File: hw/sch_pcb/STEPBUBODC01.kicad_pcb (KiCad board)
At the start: 2 copper layers, 40.1 x 30 mm, 18 parts, among them J1 HEADER_1x03, J2 HEADER_2x03_PARALLEL, J3 HEADER_1x03, J4 HEADER_1x03, J5 HEADER_2x03_PARALLEL, J6 HEADER_2x03_PARALLEL, U1 TPS631000DRLR

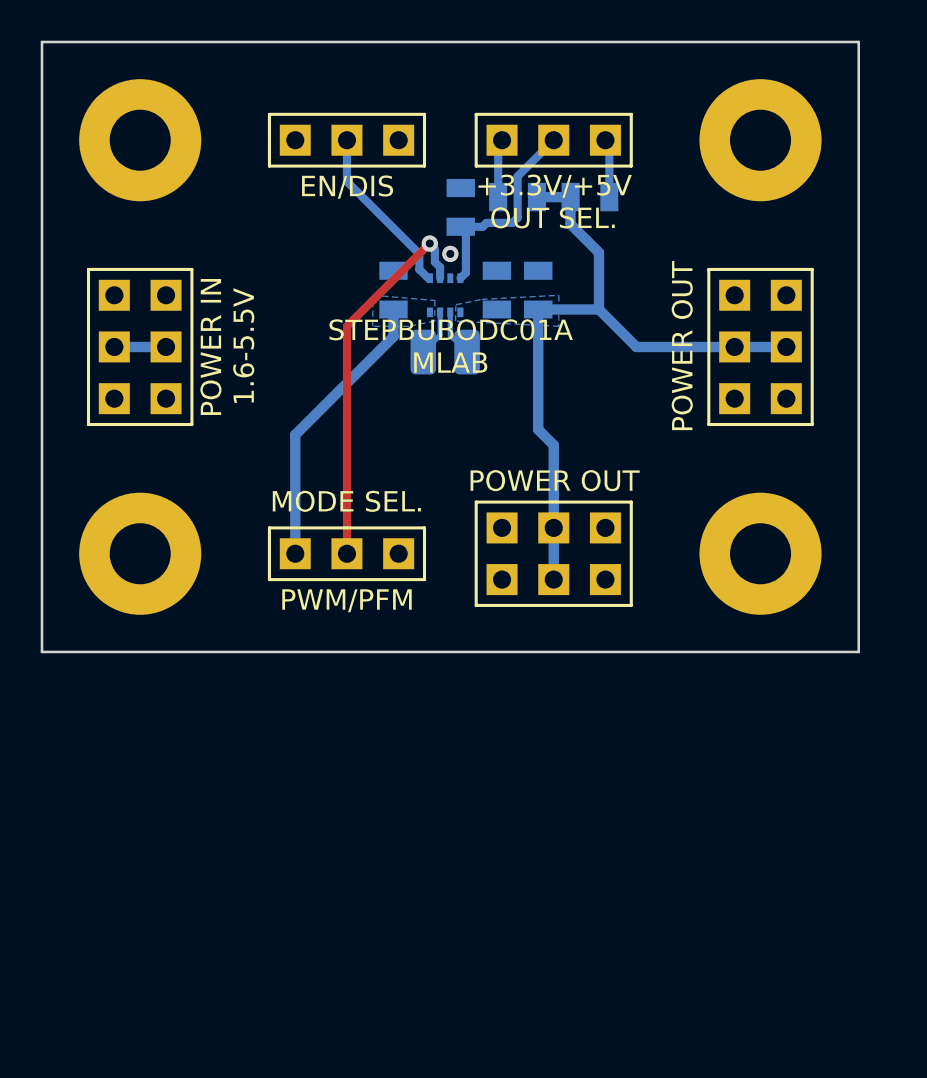
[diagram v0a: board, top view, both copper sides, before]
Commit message: Improvements in schematics and layout, solve: #1, #2, #4
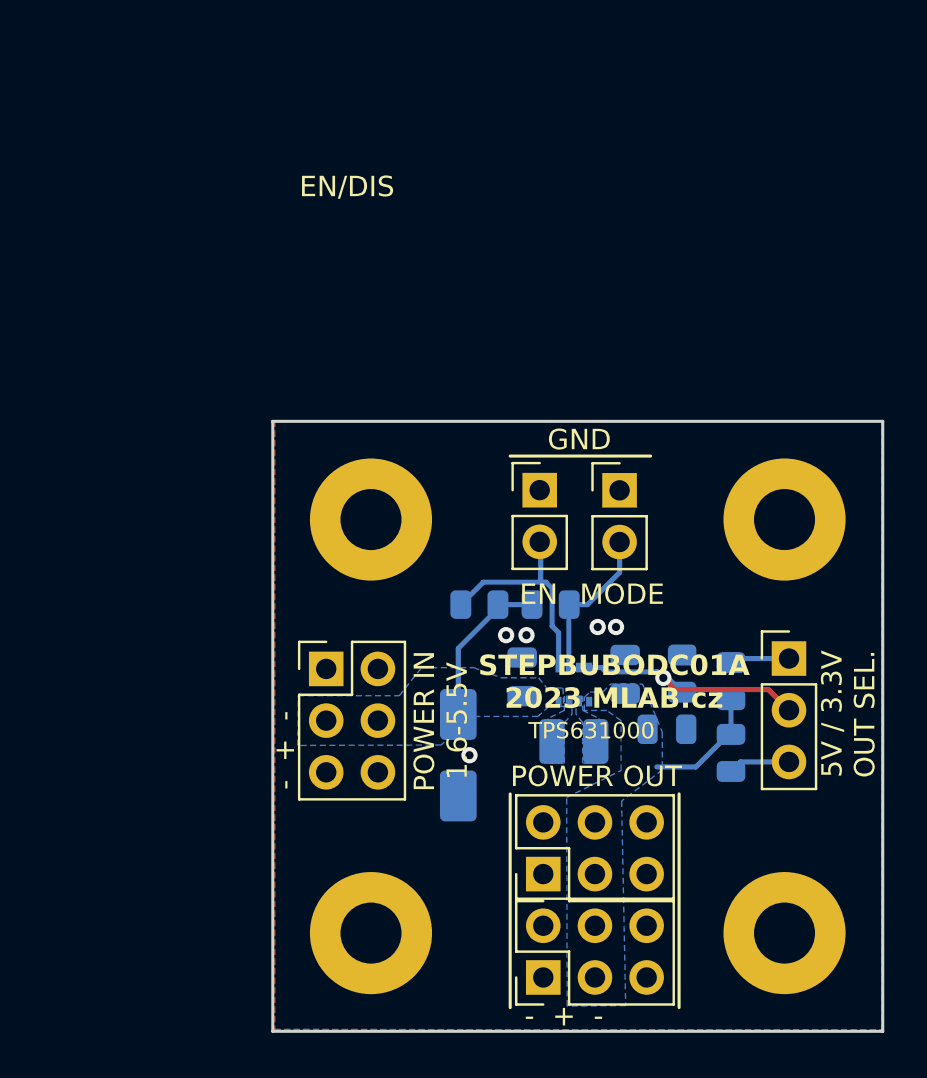
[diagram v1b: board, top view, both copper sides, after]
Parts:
- removed J1, J3: HEADER_1x03, Mlab_Pin_Headers:Straight_1x03
- added D1: M4, Diode_SMD:D_SMA, B.Cu at (142.6, 106.4)
- added JP1: Jumper_2_Open, Connector_PinHeader_2.54mm:PinHeader_1x02_P2.54mm_Vertical, F.Cu at (150.6, 93.4)
- added JP2: Jumper_2_Open, Connector_PinHeader_2.54mm:PinHeader_1x02_P2.54mm_Vertical, F.Cu at (146.6, 93.4)
- added R4: 1k, Resistor_SMD:R_0805_2012Metric, B.Cu at (147.2, 99.0)
- added R5: 1k, Resistor_SMD:R_0805_2012Metric, B.Cu at (143.7, 99.0)
- C1, C2, C3: footprint Mlab_C:SMD-0805 -> Capacitor_SMD:C_0805_2012Metric
- J2, J5, J6: footprint Mlab_Pin_Headers:Straight_2x03 -> Connector_PinHeader_2.54mm:PinHeader_2x03_P2.54mm_Vertical
- JP4: renamed from J4; footprint Mlab_Pin_Headers:Straight_1x03 -> Connector_PinHeader_2.54mm:PinHeader_1x03_P2.54mm_Vertical
- R1, R2, R3: footprint Mlab_R:SMD-0805 -> Resistor_SMD:R_0805_2012Metric
- moved H4 39.0 mm to (158.7, 115.2)
- moved R3 28.2 mm to (156.0, 106.3), turned to -90 degrees
- moved J6 28.0 mm to (146.8, 112.3), turned to 90 degrees
- moved JP4 28.0 mm to (158.9, 101.7), turned to 0 degrees
- moved R2 26.0 mm to (156.0, 102.8), turned to 90 degrees
- moved R1 25.4 mm to (153.6, 102.4)
- moved C3 22.5 mm to (152.9, 105.1), turned to 0 degrees
- moved H1 21.8 mm to (138.3, 94.8)
- moved H3 21.8 mm to (138.3, 115.2)
- moved J5 20.8 mm to (146.8, 117.3), turned to 90 degrees
- moved U1 20.1 mm to (148.3, 102.9)
- moved L1 20.1 mm to (148.3, 105.7)
- moved C1 20.0 mm to (145.8, 102.6)
- moved C2 19.9 mm to (150.8, 102.4)
- moved J2 18.3 mm to (136.1, 102.2)
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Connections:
- J2 pad 3: Net-(F1-Pad1) -> /V_in
- J2 pad 4: Net-(F1-Pad1) -> /V_in
- JP4 pad 1: Net-(J4-Pad1) -> /SEL_3v3
- JP4 pad 3: Net-(J4-Pad3) -> /SEL_5v
- R2 pad 2: Net-(J4-Pad3) -> /SEL_3v3
- R3 pad 2: Net-(J4-Pad1) -> /SEL_5v
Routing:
- net /V_out: track 34.5 -> 6.01 mm
- net /mod: track 18.8 -> 7.73 mm, vias 1 -> 0
- net /V_in: track 14.0 -> 6.59 mm
- net /SEL_5v: track 0.00 -> 3.04 mm
- net /SEL_3v3: track 0.00 -> 2.93 mm
- net Net-(J4-Pad3): track 2.87 -> 0.00 mm
- net Net-(J4-Pad1): track 2.87 -> 0.00 mm
- net Net-(F1-Pad1): track 2.54 -> 0.00 mm
- net /en: track 8.52 -> 11.0 mm
- net Net-(U1-LX2): track 2.30 -> 0.00 mm
- net Net-(U1-LX1): track 2.30 -> 0.00 mm
- net /FB: track 10.3 -> 11.9 mm, vias 0 -> 1
- net GND: track 0.00 -> 0.27 mm, vias 0 -> 5
- net (no net): vias 1 -> 0
- added copper zone on B.Cu, net GND
- added copper zone on F.Cu, net GND
- added copper zone on B.Cu, net Net-(U1-LX1)
- added copper zone on B.Cu, net Net-(U1-LX2)
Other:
- board size 40.1 x 30 mm -> 30 x 30 mm
- board text added: "- + -"
- board text added: "5V / 3.3V OUT SEL."
- board text added: "EN"
- board text added: "GND"
- board text added: "MODE"
- board text added: "STEPBUBODC01A 2023 MLAB.cz"
- board text added: "TPS631000"
- board text removed: "+3.3V/+5V OUT SEL."
- board text removed: "MODE SEL."
- board text removed: "PWM/PFM"
- board text removed: "STEPBUBODC01A MLAB"

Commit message: add fidu, check layout, drc, update ust_id
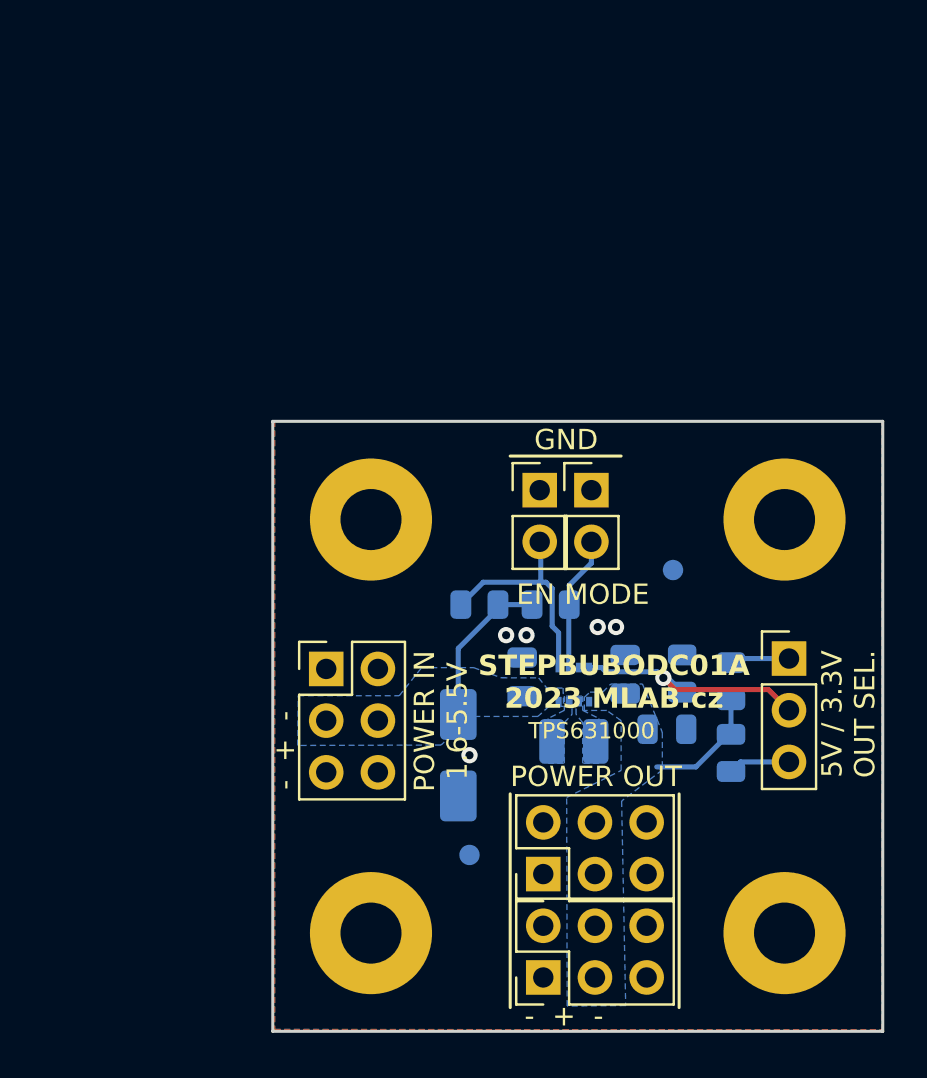
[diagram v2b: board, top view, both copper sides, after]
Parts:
- added FID1: Fiducial, Fiducial:Fiducial_1mm_Mask2mm, B.Cu at (143.2, 111.3)
- added FID2: Fiducial, Fiducial:Fiducial_1mm_Mask2mm, B.Cu at (153.2, 97.3)
- moved JP1 1.39 mm to (149.2, 93.4)
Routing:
- net /mod: track 7.73 -> 6.64 mm
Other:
- board text removed: "EN/DIS"

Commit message: Kontrola a opravy pred vyrobou
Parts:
- U1: footprint KiCad:SOTFL50P160X60-8N -> Mlab_IO:TPS631000
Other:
- rule pad_to_mask_clearance: 0 -> 0.2
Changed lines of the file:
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@@
   )
   (setup
-    (pad_to_mask_clearance 0)
+    (stackup
+      (layer "F.SilkS" (type "Top Silk Screen"))
+      (layer "F.Paste" (type "Top Solder Paste"))
+      (layer "F.Mask" (type "Top Solder Mask") (thickness 0.01))
+      (layer "F.Cu" (type "copper") (thickness 0.035))
+      (layer "dielectric 1" (type "core") (thickness 1.51) (material "FR4") (epsilon_r 4.5) (loss_tangent 0.02))
+      (layer "B.Cu" (type "copper") (thickness 0.035))
+      (layer "B.Mask" (type "Bottom Solder Mask") (thickness 0.01))
+      (layer "B.Paste" (type "Bottom Solder Paste"))
+      (layer "B.SilkS" (type "Bottom Silk Screen"))
+      (copper_finish "None")
+      (dielectric_constraints no)
+    )
+    (pad_to_mask_clearance 0.2)
     (aux_axis_origin 128.179999 125.32)
     (grid_origin 128.179999 125.32)
@@
     )
   )
-  (footprint "KiCad:SOTFL50P160X60-8N" (layer "B.Cu")
+  (footprint "Mlab_IO:TPS631000" (layer "B.Cu")
     (at 148.307999 102.949 90)
     (descr "DRL0008A")
@@
     (property "ki_description" "Switching Voltage Regulators 1.5-A output current, high power density buck-boost converter")
     (attr smd)
-    (fp_text reference "U1" (at 0 0 90) (layer "B.SilkS") hide
+    (fp_text reference "U1" (at 0 0 270) (layer "B.SilkS") hide
         (effects (font (size 1.27 1.27) (thickness 0.254)) (justify mirror))
     )
-    (fp_text value "TPS631000DRLR" (at 0 0 90) (layer "B.SilkS") hide
+    (fp_text value "TPS631000DRLR" (at 0 0 270) (layer "B.SilkS") hide
         (effects (font (size 1.27 1.27) (thickness 0.254)) (justify mirror))
     )
-    (fp_text user "${REFERENCE}" (at 0 0 90) (layer "B.Fab")
+    (fp_text user "${REFERENCE}" (at 0 0 270) (layer "B.Fab")
         (effects (font (size 1.27 1.27) (thickness 0.254)) (justify mirror))
     )
@@
     (fp_line (start 0.6 1.05) (end 0.6 -1.05)
       (stroke (width 0.1) (type solid)) (layer "B.Fab"))
-    (pad "1" smd rect (at -0.838 0.75) (size 0.3 0.475) (layers "B.Cu" "B.Paste" "B.Mask")
+    (pad "1" smd rect (at -0.74 0.75) (size 0.3 0.67) (layers "B.Cu" "B.Paste" "B.Mask")
       (net 3 "/V_out") (pinfunction "VOUT") (pintype "passive"))
-    (pad "2" smd rect (at -0.838 0.25) (size 0.3 0.475) (layers "B.Cu" "B.Paste" "B.Mask")
+    (pad "2" smd rect (at -0.74 0.25) (size 0.3 0.67) (layers "B.Cu" "B.Paste" "B.Mask")
       (net 8 "Net-(U1-LX2)") (pinfunction "LX2") (pintype "passive"))
-    (pad "3" smd rect (at -0.838 -0.25) (size 0.3 0.475) (layers "B.Cu" "B.Paste" "B.Mask")
+    (pad "3" smd rect (at -0.74 -0.25) (size 0.3 0.67) (layers "B.Cu" "B.Paste" "B.Mask")
       (net 7 "Net-(U1-LX1)") (pinfunction "LX1") (pintype "passive"))
-    (pad "4" smd rect (at -0.838 -0.75) (size 0.3 0.475) (layers "B.Cu" "B.Paste" "B.Mask")
+    (pad "4" smd rect (at -0.74 -0.75) (size 0.3 0.67) (layers "B.Cu" "B.Paste" "B.Mask")
       (net 1 "/V_in") (pinfunction "VIN") (pintype "passive"))
-    (pad "5" smd rect (at 0.838 -0.75) (size 0.3 0.475) (layers "B.Cu" "B.Paste" "B.Mask")
+    (pad "5" smd rect (at 0.74 -0.75) (size 0.3 0.67) (layers "B.Cu" "B.Paste" "B.Mask")
       (net 4 "/en") (pinfunction "EN") (pintype "passive"))
-    (pad "6" smd rect (at 0.838 -0.25) (size 0.3 0.475) (layers "B.Cu" "B.Paste" "B.Mask")
+    (pad "6" smd rect (at 0.74 -0.25) (size 0.3 0.67) (layers "B.Cu" "B.Paste" "B.Mask")
       (net 5 "/mod") (pinfunction "MODE") (pintype "passive"))
-    (pad "7" smd rect (at 0.838 0.25) (size 0.3 0.475) (layers "B.Cu" "B.Paste" "B.Mask")
+    (pad "7" smd rect (at 0.74 0.25) (size 0.3 0.67) (layers "B.Cu" "B.Paste" "B.Mask")
       (net 2 "GND") (pinfunction "GND") (pintype "passive"))
-    (pad "8" smd rect (at 0.838 0.75) (size 0.3 0.475) (layers "B.Cu" "B.Paste" "B.Mask")
+    (pad "8" smd rect (at 0.74 0.75) (size 0.3 0.67) (layers "B.Cu" "B.Paste" "B.Mask")
       (net 6 "/FB") (pinfunction "FB") (pintype "passive"))
     (model "TPS631000DRLR.stp"
